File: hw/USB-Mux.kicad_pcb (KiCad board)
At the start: 4 copper layers, 60 x 70 mm, 89 parts, among them J101 USB-61400416121, J102 USB-676432911, J103 USB-61400416121, J104 USB-676432911, J201 Conn_01x08, J202 Molex-105017-0001, P201 Current-Probe, Q101 DTC114EE, Q102 DTC114EE, Q103 DTC114EE, Q104 DTC114EE, Q201 DTC114EE, U101 TS3USB221, U102 TS3USB221, U103 TPS22976, U104 TPS22976, U201 STM32F401XX-LQFP64, U202 TLV62150A, X101 Lightpipe-5x12.7mm-Dome, X102 Lightpipe-5x12.7mm-Dome, X103 Lightpipe-5x12.7mm-Dome, X104 Lightpipe-5x12.7mm-Dome, X105 Lightpipe-5x12.7mm-Dome, X201 Mounting-Hole-M3, X202 Mounting-Hole-M3, X203 Mounting-Hole-M3, X204 Mounting-Hole-M3, Y201 MCSJK-7I-8.00-18-30-60-B-30

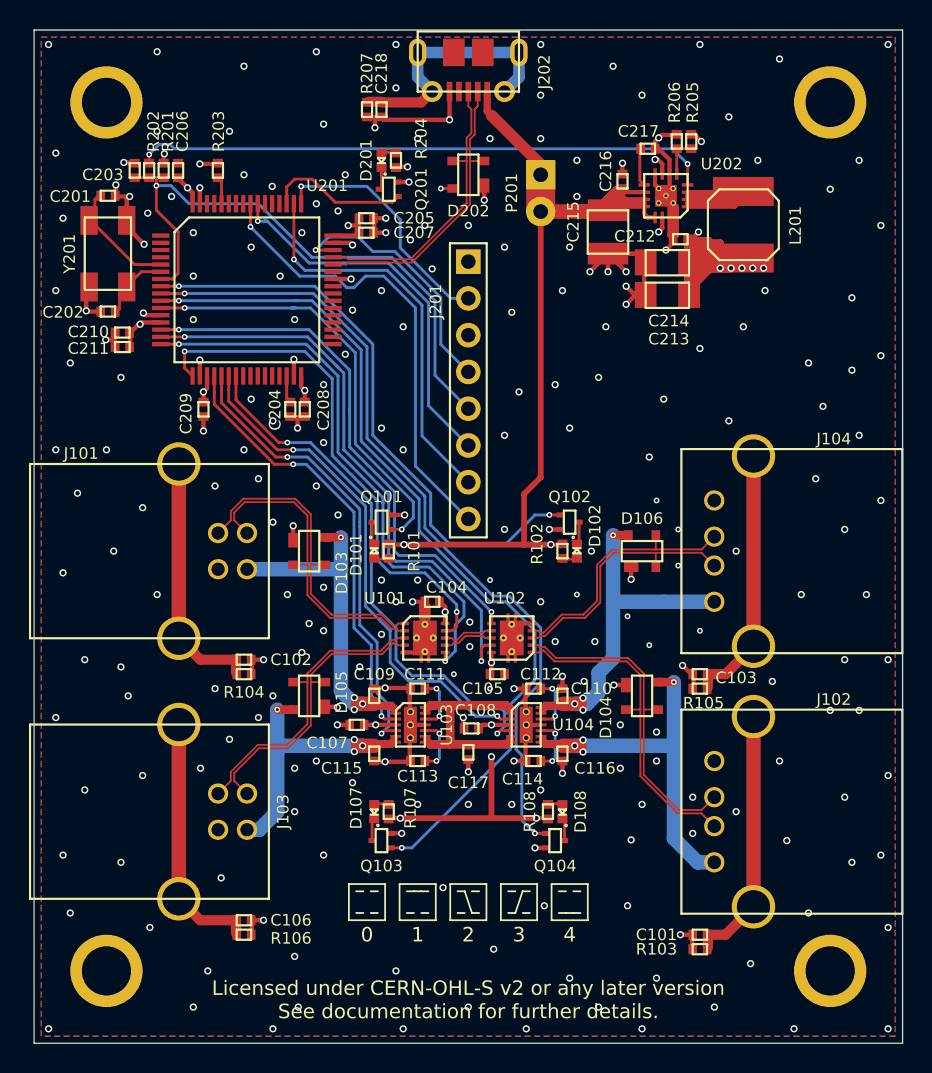
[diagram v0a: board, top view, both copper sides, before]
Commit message: Layout USB-Mux rev2.
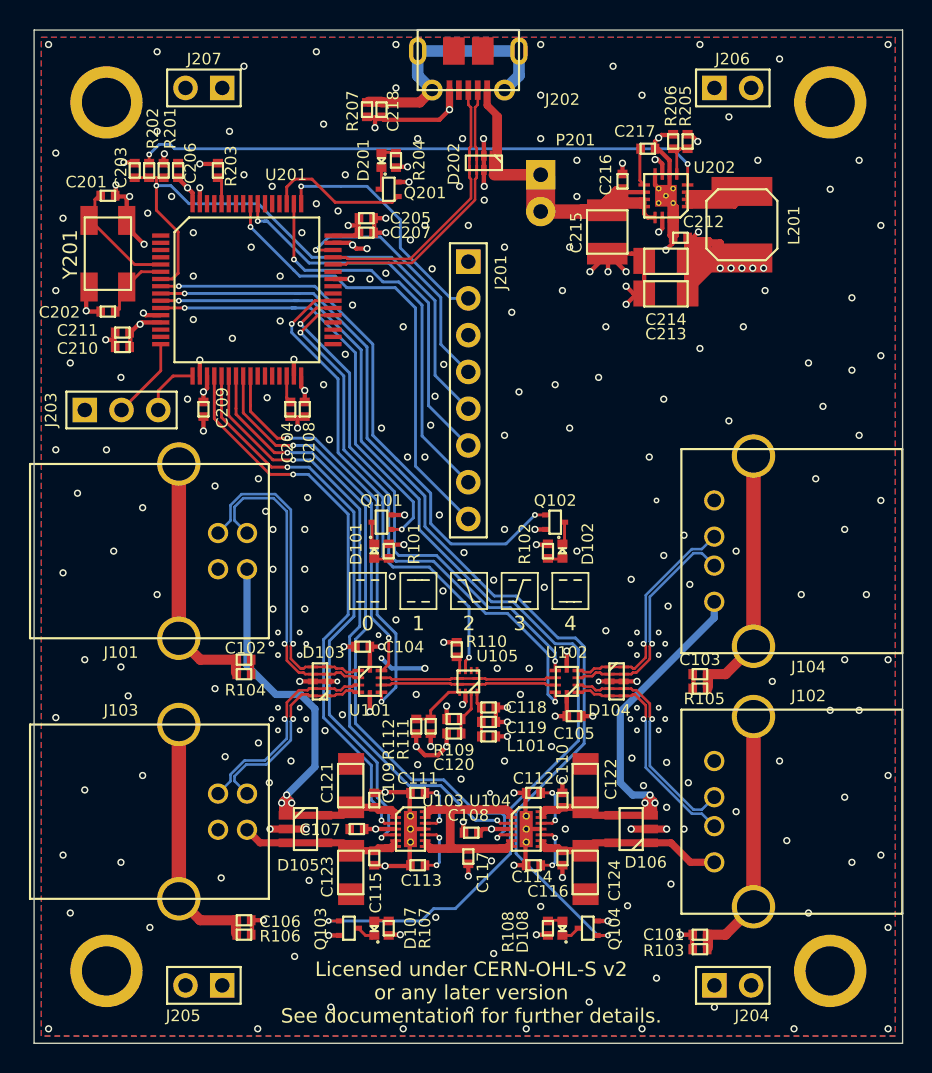
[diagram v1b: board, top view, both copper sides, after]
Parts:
- added C118: 100nF_16V, USB-Mux:C_0402, F.Cu at (111.4, 66.8)
- added C119: 1.0uF_6.3V, USB-Mux:C_0402, F.Cu at (111.4, 67.8)
- added C120: 100nF_16V, USB-Mux:C_0402, F.Cu at (109.0, 68.6)
- added C121: 22uF_25V, USB-Mux:C_1206, F.Cu at (101.9, 72.2)
- added C122: 22uF_25V, USB-Mux:C_1206, F.Cu at (118.1, 72.2)
- added C123: 22uF_25V, USB-Mux:C_1206, F.Cu at (101.9, 78.2)
- added C124: 22uF_25V, USB-Mux:C_1206, F.Cu at (118.1, 78.2)
- added J203: Conn_01x03, USB-Mux:Pin_Header_Straight_1x03_Pitch2.54mm, F.Cu at (83.5, 46.2)
- added J204: Conn_01x02, USB-Mux:Pin_Header_Straight_1x02_Pitch2.54mm, F.Cu at (127.0, 86.0)
- added J205: Conn_01x02, USB-Mux:Pin_Header_Straight_1x02_Pitch2.54mm, F.Cu at (93.0, 86.0)
- added J206: Conn_01x02, USB-Mux:Pin_Header_Straight_1x02_Pitch2.54mm, F.Cu at (127.0, 24.0)
- added J207: Conn_01x02, USB-Mux:Pin_Header_Straight_1x02_Pitch2.54mm, F.Cu at (93.0, 24.0)
- added L101: BLM15PE121SH1D, USB-Mux:L_0402, F.Cu at (111.4, 68.8)
- added R109: dnp, USB-Mux:R_0402, F.Cu at (109.0, 67.6)
- added R110: dnp, USB-Mux:R_0402, F.Cu at (109.2, 62.8)
- added R111: 28k0 (dnp), USB-Mux:R_0402, F.Cu at (107.4, 68.1)
- added R112: 28k0 (dnp), USB-Mux:R_0402, F.Cu at (106.4, 68.1)
- added U105: TUSB212, USB-Mux:X2QFN12-RWB, F.Cu at (110.0, 65.0)
- D103, D104, D202: value SP0503BAHTG -> TPD4E02B04; footprint USB-Mux:SOT-143 -> USB-Mux:USON10
- D105, D106: value SP0503BAHTG -> ESDS302; footprint USB-Mux:SOT-143 -> USB-Mux:SOT-23-5
- U101, U102: value TS3USB221 -> TS3USB3000; footprint USB-Mux:VSON10 -> USB-Mux:UQFN10-RSE
- moved D106 19.2 mm to (121.2, 75.2), turned to 180 degrees
- moved D105 9.20 mm to (98.8, 75.2), turned to 0 degrees
- moved D103 9.03 mm to (99.8, 65.0), turned to 180 degrees
- moved D107 8.05 mm to (103.5, 82.0)
- moved D108 8.05 mm to (116.5, 82.0)
- moved R107 8.05 mm to (104.5, 82.0)
- moved R108 8.05 mm to (115.5, 82.0)
- moved X104 8.05 mm to (103.5, 82.0)
- moved X105 8.05 mm to (116.5, 82.0)
- moved C107 7.20 mm to (102.3, 75.2)
- moved C108 7.20 mm to (110.2, 75.5)
- moved C109 7.20 mm to (103.5, 73.2)
- moved C110 7.20 mm to (116.5, 73.2)
- moved C111 7.20 mm to (106.5, 72.7)
- moved C112 7.20 mm to (114.5, 72.7)
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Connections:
- D103 pad 1: GND -> /IN1_DN
- D103 pad 2: /IN0_DN -> /IN1_DP
- D103 pad 3: /IN0_DP -> GND
- D103 pad 4: /VBUS_IN0 -> /IN0_DN
- D104 pad 1: GND -> /OUT1_DP
- D104 pad 2: /OUT0_DN -> /OUT1_DN
- D104 pad 3: /OUT0_DP -> GND
- D104 pad 4: /VBUS_OUT0 -> /OUT0_DP
- D105 pad 1: GND -> /VBUS_IN0
- D105 pad 2: /IN1_DN -> GND
- D105 pad 3: /IN1_DP -> /VBUS_IN1
- D106 pad 1: GND -> /VBUS_OUT0
- D106 pad 2: /OUT1_DN -> GND
- D106 pad 3: /OUT1_DP -> /VBUS_OUT1
- D202 pad 1: GND -> /Controller/VBUS
- D202 pad 2: /Controller/USB_DN -> /Controller/VBUS
- D202 pad 3: /Controller/USB_DP -> GND
- D202 pad 4: VDD_5V0 -> /Controller/USB_DN
- J202 pad 1: VDD_5V0 -> /Controller/VBUS
- J202 pad 4: Net-(J202-Pad4) -> (no net)
- P201 pad 1: VDD_5V0 -> /Controller/VBUS
- U101 pad 7: /X_DP -> /X_DN
- U101 pad 8: /X_DN -> /X_DP
- U102 pad 7: /X_DN -> /X_DP
- U102 pad 8: /X_DP -> /X_DN
- U201 pad 1: Net-(U201-Pad1) -> (no net)
- U201 pad 14: /MUX_EN1 -> (no net)
- U201 pad 15: /MUX1 -> (no net)
- U201 pad 16: /MUX_EN0 -> /Controller/TX
- U201 pad 17: /MUX0 -> /Controller/RX
- U201 pad 2: Net-(U201-Pad2) -> (no net)
- U201 pad 24: Net-(U201-Pad24) -> /MUX0
- U201 pad 25: Net-(U201-Pad25) -> /MUX_EN0
- U201 pad 26: Net-(U201-Pad26) -> (no net)
- U201 pad 27: Net-(U201-Pad27) -> (no net)
- U201 pad 28: Net-(U201-Pad28) -> (no net)
- U201 pad 29: Net-(U201-Pad29) -> (no net)
- U201 pad 3: Net-(U201-Pad3) -> (no net)
- U201 pad 33: Net-(U201-Pad33) -> (no net)
- U201 pad 34: Net-(U201-Pad34) -> (no net)
- U201 pad 35: Net-(U201-Pad35) -> (no net)
- U201 pad 36: Net-(U201-Pad36) -> (no net)
- U201 pad 37: Net-(U201-Pad37) -> /MUX1
- U201 pad 38: Net-(U201-Pad38) -> /MUX_EN1
- U201 pad 39: Net-(U201-Pad39) -> /BOOST_EN
- U201 pad 4: Net-(U201-Pad4) -> (no net)
- U201 pad 40: Net-(U201-Pad40) -> (no net)
- U201 pad 41: Net-(U201-Pad41) -> (no net)
- U201 pad 43: Net-(U201-Pad43) -> (no net)
- U201 pad 52: Net-(U201-Pad52) -> (no net)
- U201 pad 53: Net-(U201-Pad53) -> (no net)
- U201 pad 54: Net-(U201-Pad54) -> (no net)
- U201 pad 57: Net-(U201-Pad57) -> (no net)
- U201 pad 58: Net-(U201-Pad58) -> (no net)
- U201 pad 59: Net-(U201-Pad59) -> (no net)
- U201 pad 61: Net-(U201-Pad61) -> (no net)
- U201 pad 62: Net-(U201-Pad62) -> (no net)
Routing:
- net /BOOST_EN: track 0.00 -> 34.2 mm, vias 0 -> 2
- net GND: track 1313.4 -> 1332.7 mm, vias 246 -> 283
- net /VBUS_IN0: track 26.4 -> 41.5 mm, vias 4 -> 3
- net /Controller/VBUS: track 0.00 -> 14.8 mm
- net /LED_IN1: track 60.4 -> 75.2 mm
- net /LED_OUT1: track 57.2 -> 70.2 mm
- net /VBUS_OUT0: track 28.6 -> 16.4 mm, vias 4 -> 0
- net /VBUS_OUT1: track 27.8 -> 39.8 mm, vias 4 -> 3
- net VDD_3V3: track 198.5 -> 209.7 mm, vias 18 -> 21
- net /MUX_EN0: track 39.2 -> 29.3 mm
- net /MUX0: track 35.9 -> 26.3 mm
- net /PWR_EN0: track 30.6 -> 39.5 mm
- net /PWR_EN1: track 32.0 -> 40.9 mm
- net /X_DP: track 3.52 -> 12.1 mm
- net /X_DN: track 3.52 -> 12.1 mm
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- added copper zone on In4.Cu, net GND
- added copper zone on In3.Cu, net VDD_5V0
- removed copper zone on In2.Cu, net VDD_5V0
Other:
- copper layers 4 -> 6
- net class USB: clearance 0.1 -> 0.2; trace_width 0.13 -> 0.18
- board text added: "PCB Stack-Up: Top Layer: 35 um 2x Prepreg 2116: 230 um Inner Layer 1: 35 um Core: 300 um Inner Layer 2: 35 um 3x Prepreg 2116: 340um Inner Layer 3: 35 um Core: 300 um Inner Layer 4: 35 um 2x Prepreg 2116: 230um Bottom Layer: 35 um εr_FR4 = 4.3 εr_soldermask = 3.2 USB-Trace: width = 180 um spacing = 100 um gnd_spacing = 200 um Zdiff = 93.584 Ω Zcomm = 43.745 Ω"
- board text removed: "PCB Stack-Up: Top Layer: 35 um 2x Prepreg 1080: 140um Inner Layer 1: 35 um Core: 1200 um Inner Layer 2: 35 um 2x Prepreg 1080: 140um Bottom Layer: 35 um εr_FR4 = 4.3 εr_soldermask = 3.2 USB-Trace: width = 130 um spacing = 100 um Zdiff = 97.394 Ω Zcomm = 40.137 Ω"

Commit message: Update project to KiCad 6 file formats.
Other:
- net class Default removed
- net class Power removed
- net class USB removed

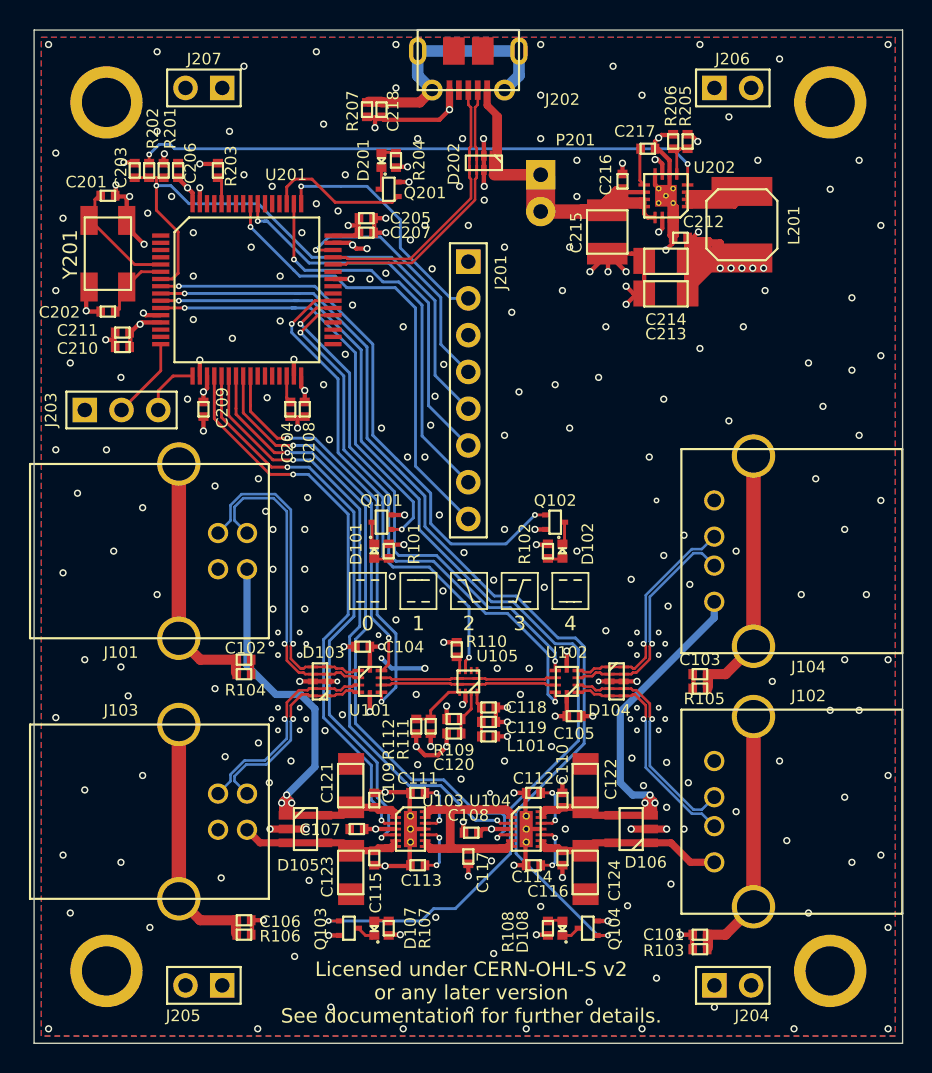
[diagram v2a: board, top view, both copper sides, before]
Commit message: Improve Layout, use impedances from manufacturer.
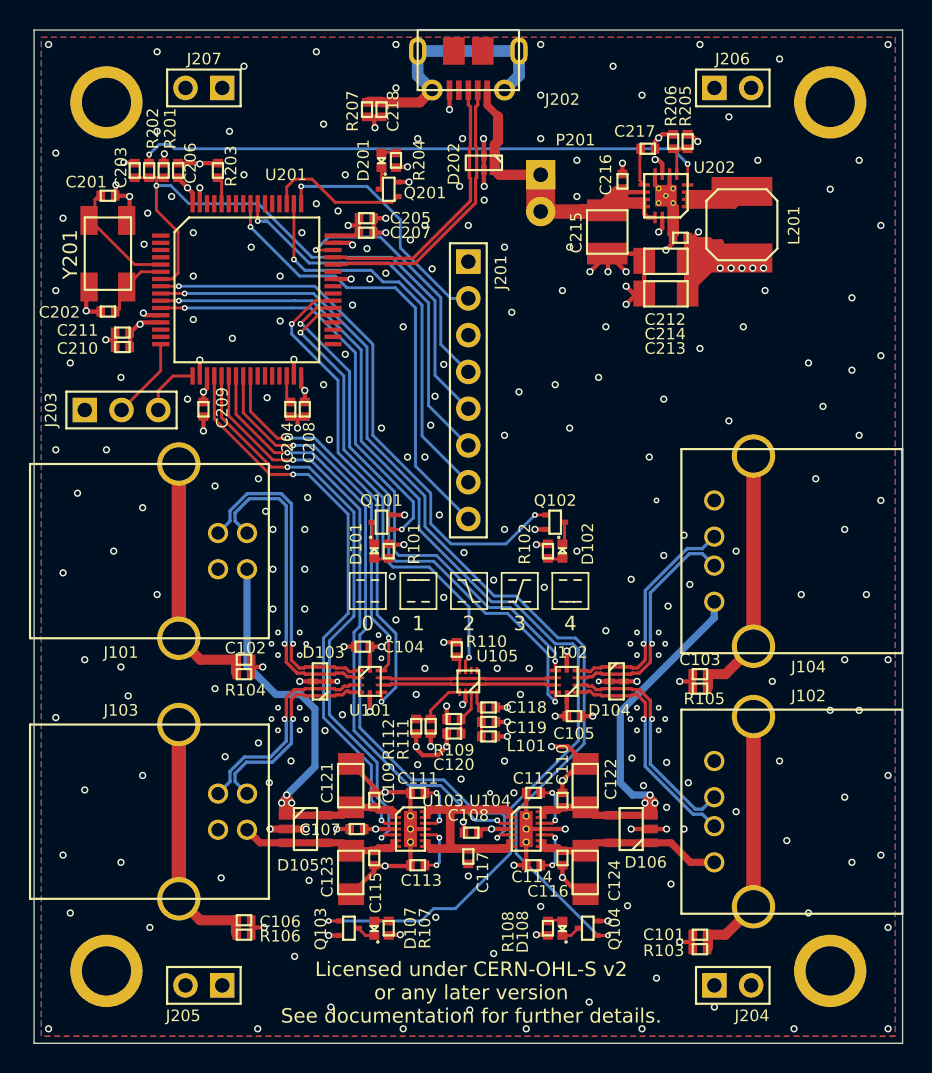
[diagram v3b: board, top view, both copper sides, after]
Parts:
- R101, R107: value 750 -> 750R
- R102, R108: value 1K58 -> 1.58kR
- R103, R104, R105, R106, R207: value 1M0 -> 1.0MR
- R109, R110: value dnp -> 0.0R (dnp)
- R111, R112: value 28k0 (dnp) -> 28.0kR (dnp)
- R201, R203: value 10K0 -> 10.0kR
- R202: value 0R0 -> 0.0R
- R204: value 1K0 -> 1.0kR
- R205: value 71K5 -> 71.5kR
- R206: value 22K6 -> 22.6kR
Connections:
- J202 pad 4: (no net) -> unconnected-(J202-Pad4)
- U105 pad 3: (no net) -> unconnected-(U105-Pad3)
- U105 pad 4: (no net) -> unconnected-(U105-Pad4)
- U201 pad 1: (no net) -> unconnected-(U201-Pad1)
- U201 pad 14: (no net) -> unconnected-(U201-Pad14)
- U201 pad 15: (no net) -> unconnected-(U201-Pad15)
- U201 pad 2: (no net) -> unconnected-(U201-Pad2)
- U201 pad 26: (no net) -> unconnected-(U201-Pad26)
- U201 pad 27: (no net) -> unconnected-(U201-Pad27)
- U201 pad 28: (no net) -> unconnected-(U201-Pad28)
- U201 pad 29: (no net) -> unconnected-(U201-Pad29)
- U201 pad 3: (no net) -> unconnected-(U201-Pad3)
- U201 pad 33: (no net) -> unconnected-(U201-Pad33)
- U201 pad 34: (no net) -> unconnected-(U201-Pad34)
- U201 pad 35: (no net) -> unconnected-(U201-Pad35)
- U201 pad 36: (no net) -> unconnected-(U201-Pad36)
- U201 pad 4: (no net) -> unconnected-(U201-Pad4)
- U201 pad 40: (no net) -> unconnected-(U201-Pad40)
- U201 pad 41: (no net) -> unconnected-(U201-Pad41)
- U201 pad 43: (no net) -> unconnected-(U201-Pad43)
- U201 pad 52: (no net) -> unconnected-(U201-Pad52)
- U201 pad 53: (no net) -> unconnected-(U201-Pad53)
- U201 pad 54: (no net) -> unconnected-(U201-Pad54)
- U201 pad 57: (no net) -> unconnected-(U201-Pad57)
- U201 pad 58: (no net) -> unconnected-(U201-Pad58)
- U201 pad 59: (no net) -> unconnected-(U201-Pad59)
- U201 pad 61: (no net) -> unconnected-(U201-Pad61)
- U201 pad 62: (no net) -> unconnected-(U201-Pad62)
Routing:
- net GND: track 1332.7 -> 492.4 mm, vias 283 -> 286
- net /Controller/VBUS: track 14.8 -> 9.24 mm
- net VDD_3V3: track 209.7 -> 208.6 mm, vias 21 -> 20
- net VDD_5V0: vias 9 -> 8
